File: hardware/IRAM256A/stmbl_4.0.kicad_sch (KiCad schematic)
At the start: 2 parts

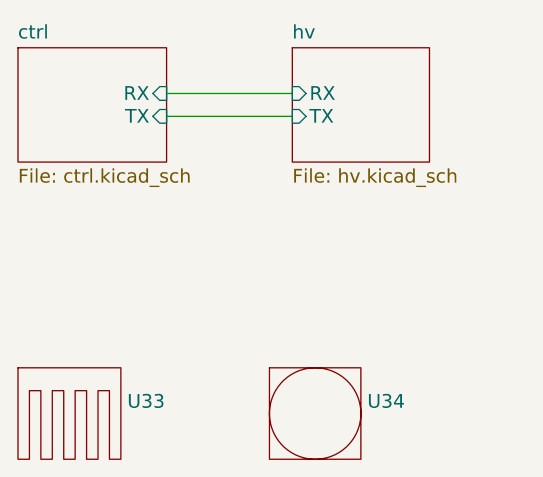
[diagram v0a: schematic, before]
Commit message: Structure change + kicad 3d models updated
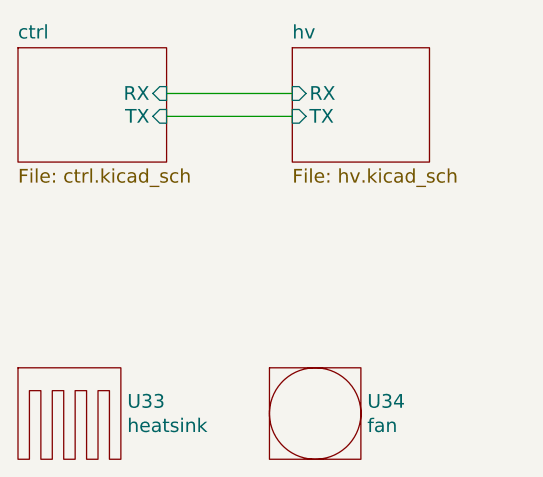
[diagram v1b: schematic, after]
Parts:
- U33: value (none) -> heatsink
- U34: value (none) -> fan
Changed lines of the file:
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@@
       (effects (font (size 1.524 1.524)) (justify left))
     )
-    (property "Value" "" (id 1) (at 121.3612 100.4062 0)
+    (property "Value" "heatsink" (id 1) (at 121.3612 100.4062 0)
       (effects (font (size 1.524 1.524)) (justify left))
     )
@@
       (effects (font (size 1.524 1.524)) (justify left))
     )
-    (property "Value" "" (id 1) (at 148.0312 100.4062 0)
+    (property "Value" "fan" (id 1) (at 148.0312 100.4062 0)
       (effects (font (size 1.524 1.524)) (justify left))
     )
@@
     )
     (path "/00000000-0000-0000-0000-000056590966/00000000-0000-0000-0000-000056591923/00000000-0000-0000-0000-00005700ea19"
-      (reference "Q1") (unit 1) (value "IRLML6344") (footprint "stmbl:SOT-23")
+      (reference "Q1") (unit 1) (value "IRLML6344") (footprint "SOT-23")
     )
     (path "/00000000-0000-0000-0000-000056590966/00000000-0000-0000-0000-000056591923/00000000-0000-0000-0000-000057011943"
-      (reference "Q2") (unit 1) (value "IRLML6344") (footprint "stmbl:SOT-23")
+      (reference "Q2") (unit 1) (value "IRLML6344") (footprint "SOT-23")
     )
     (path "/00000000-0000-0000-0000-000056590966/00000000-0000-0000-0000-000056591923/00000000-0000-0000-0000-0000570122c9"
-      (reference "Q3") (unit 1) (value "IRLML6344") (footprint "stmbl:SOT-23")
+      (reference "Q3") (unit 1) (value "IRLML6344") (footprint "SOT-23")
     )
     (path "/00000000-0000-0000-0000-000056590966/00000000-0000-0000-0000-000056591923/00000000-0000-0000-0000-000057014d91"
-      (reference "Q4") (unit 1) (value "IRLML6344") (footprint "stmbl:SOT-23")
+      (reference "Q4") (unit 1) (value "IRLML6344") (footprint "SOT-23")
     )
     (path "/00000000-0000-0000-0000-00005659094d/00000000-0000-0000-0000-00005b2ee5f2"
-      (reference "Q5") (unit 1) (value "IRLML6344") (footprint "stmbl:SOT-23")
+      (reference "Q5") (unit 1) (value "IRLML6344") (footprint "SOT-23")
     )
     (path "/00000000-0000-0000-0000-000056590966/00000000-0000-0000-0000-000056591913/00000000-0000-0000-0000-000056602deb"
@@
     )
     (path "/00000000-0000-0000-0000-000056590966/00000000-0000-0000-0000-000056591919/00000000-0000-0000-0000-0000565dd0e7"
-      (reference "U8") (unit 1) (value "SN65176B") (footprint "stmbl:SOIC-8-N")
+      (reference "U8") (unit 1) (value "SN65176B") (footprint "SO-8")
     )
     (path "/00000000-0000-0000-0000-000056590966/00000000-0000-0000-0000-000056591919/00000000-0000-0000-0000-0000565ddc9b"
-      (reference "U9") (unit 1) (value "SN65176B") (footprint "stmbl:SOIC-8-N")
+      (reference "U9") (unit 1) (value "SN65176B") (footprint "SO-8")
     )
     (path "/00000000-0000-0000-0000-000056590966/00000000-0000-0000-0000-000056591919/00000000-0000-0000-0000-0000565ddf06"
-      (reference "U10") (unit 1) (value "SN65176B") (footprint "stmbl:SOIC-8-N")
+      (reference "U10") (unit 1) (value "SN65176B") (footprint "SO-8")
     )
     (path "/00000000-0000-0000-0000-000056590966/00000000-0000-0000-0000-000056591919/00000000-0000-0000-0000-0000565ddf3c"
-      (reference "U11") (unit 1) (value "SN65176B") (footprint "stmbl:SOIC-8-N")
+      (reference "U11") (unit 1) (value "SN65176B") (footprint "SO-8")
     )
     (path "/00000000-0000-0000-0000-00005659094d/00000000-0000-0000-0000-000056590a75/00000000-0000-0000-0000-00005668dd3b"
@@
     )
     (path "/00000000-0000-0000-0000-000056590966/00000000-0000-0000-0000-00005659191c/00000000-0000-0000-0000-0000565dfe81"
-      (reference "U14") (unit 1) (value "SN65176B") (footprint "stmbl:SOIC-8-N")
+      (reference "U14") (unit 1) (value "SN65176B") (footprint "SO-8")
     )
     (path "/00000000-0000-0000-0000-000056590966/00000000-0000-0000-0000-0000565f7162/00000000-0000-0000-0000-0000565dfe81"
-      (reference "U15") (unit 1) (value "SN65176B") (footprint "stmbl:SOIC-8-N")
+      (reference "U15") (unit 1) (value "SN65176B") (footprint "SO-8")
     )
     (path "/00000000-0000-0000-0000-000056590966/00000000-0000-0000-0000-0000565f7162/00000000-0000-0000-0000-0000565dfeac"
-      (reference "U16") (unit 1) (value "SN65176B") (footprint "stmbl:SOIC-8-N")
+      (reference "U16") (unit 1) (value "SN65176B") (footprint "SO-8")
     )
     (path "/00000000-0000-0000-0000-000056590966/00000000-0000-0000-0000-00005659191c/00000000-0000-0000-0000-0000565dfeac"
-      (reference "U17") (unit 1) (value "SN65176B") (footprint "stmbl:SOIC-8-N")
+      (reference "U17") (unit 1) (value "SN65176B") (footprint "SO-8")
     )
     (path "/00000000-0000-0000-0000-000056590966/00000000-0000-0000-0000-00005659191c/00000000-0000-0000-0000-0000565dfed0"
-      (reference "U18") (unit 1) (value "SN65176B") (footprint "stmbl:SOIC-8-N")
+      (reference "U18") (unit 1) (value "SN65176B") (footprint "SO-8")
     )
     (path "/00000000-0000-0000-0000-000056590966/00000000-0000-0000-0000-0000565f7162/00000000-0000-0000-0000-0000565dfed0"
-      (reference "U19") (unit 1) (value "SN65176B") (footprint "stmbl:SOIC-8-N")
+      (reference "U19") (unit 1) (value "SN65176B") (footprint "SO-8")
     )
     (path "/00000000-0000-0000-0000-000056590966/00000000-0000-0000-0000-000056591913/00000000-0000-0000-0000-00005818acd9"
@@
     )
     (path "/00000000-0000-0000-0000-00005659094d/00000000-0000-0000-0000-0000565909d0/00000000-0000-0000-0000-0000570da682"
-      (reference "U25") (unit 1) (value "STM32F303CBTx") (footprint "stmbl:LQFP-48_7x7mm_Pitch0.5mm")
+      (reference "U25") (unit 1) (value "STM32F303CBTx") (footprint "LQFP48")
     )
     (path "/00000000-0000-0000-0000-000056590966/00000000-0000-0000-0000-000056591913/00000000-0000-0000-0000-0000565fd974"
-      (reference "U26") (unit 1) (value "STM32F405VG") (footprint "stmbl:LQFP-100_14x14mm_Pitch0.5mm")
+      (reference "U26") (unit 1) (value "STM32F405VG") (footprint "TQFP100")
     )
     (path "/00000000-0000-0000-0000-000056590966/00000000-0000-0000-0000-000056591916/00000000-0000-0000-0000-000057ad27cc"
